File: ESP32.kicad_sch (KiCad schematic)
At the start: 5 parts, among them U6 ESP32-WROOM-32

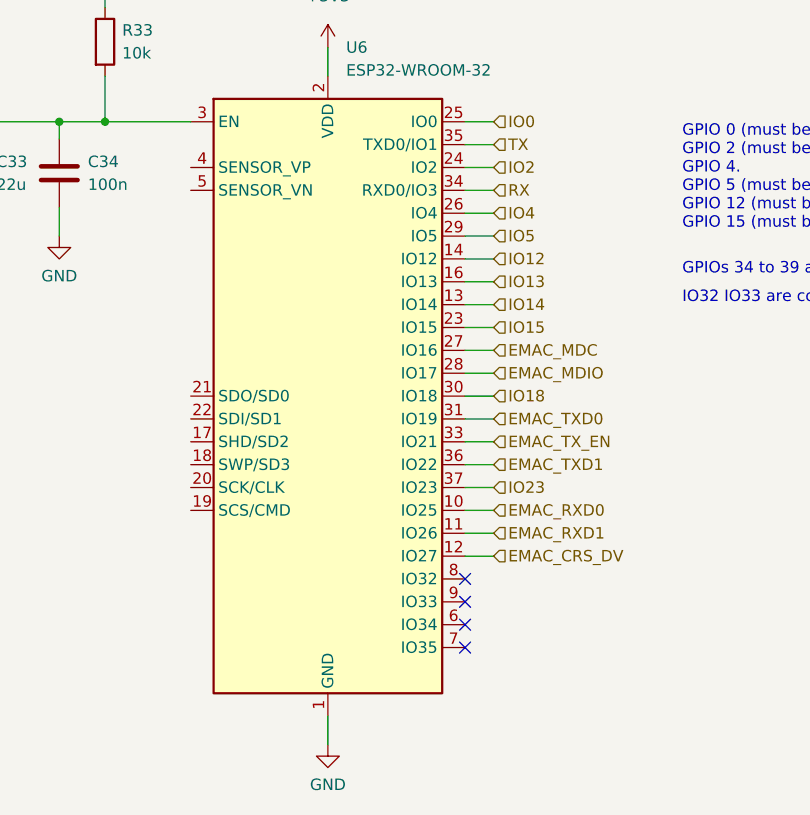
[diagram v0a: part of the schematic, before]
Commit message: Update schematic for V1.1
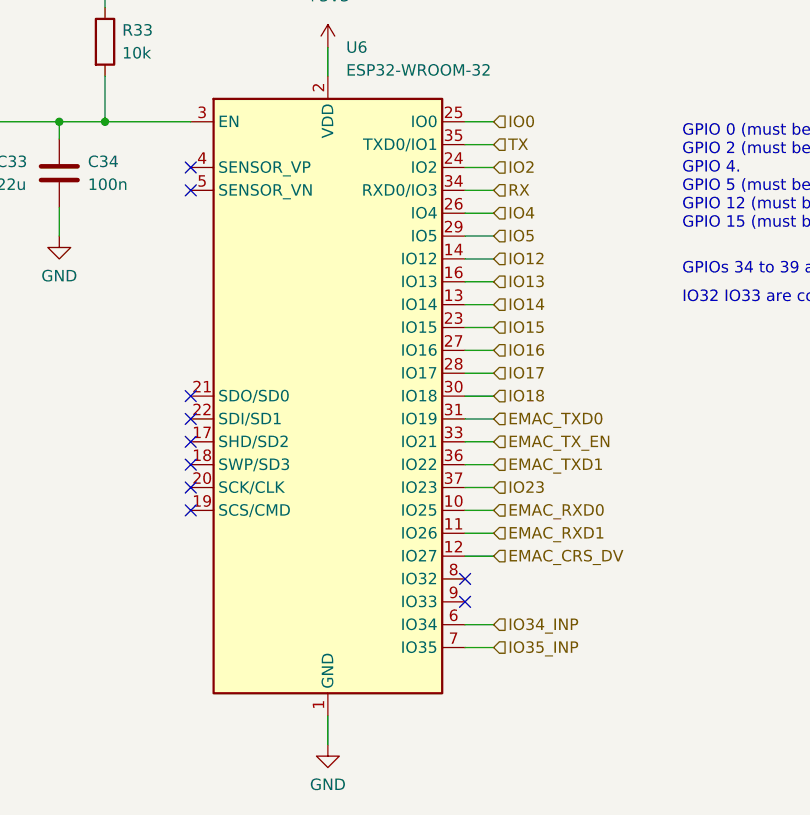
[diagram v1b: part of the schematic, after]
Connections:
- net IO34_INP: now reaches U6.6 (IO34)
- net IO35_INP: now reaches U6.7 (IO35)
- net EMAC_MDC renamed IO16
- net EMAC_MDIO renamed IO17
- no-connect marks 4 -> 10
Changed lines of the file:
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@@
 	)
 	(no_connect
-		(at 160.02 119.38)
-	)
-	(no_connect
-		(at 160.02 121.92)
+		(at 129.54 96.52)
+	)
+	(no_connect
+		(at 129.54 104.14)
 	)
 	(no_connect
@@
 	)
 	(no_connect
+		(at 129.54 101.6)
+	)
+	(no_connect
+		(at 129.54 71.12)
+	)
+	(no_connect
+		(at 129.54 93.98)
+	)
+	(no_connect
+		(at 129.54 106.68)
+	)
+	(no_connect
 		(at 160.02 114.3)
 	)
+	(no_connect
+		(at 129.54 99.06)
+	)
+	(no_connect
+		(at 129.54 68.58)
+	)
 	(wire
 		(pts
@@
 	(wire
 		(pts
+			(xy 163.195 121.92) (xy 160.02 121.92)
+		)
+		(stroke
+			(width 0)
+			(type default)
+		)
+	)
+	(wire
+		(pts
 			(xy 160.02 83.82) (xy 163.195 83.82)
+		)
+		(stroke
+			(width 0)
+			(type default)
+		)
+	)
+	(wire
+		(pts
+			(xy 160.02 119.38) (xy 163.195 119.38)
 		)
 		(stroke
@@
 		)
 	)
+	(hierarchical_label "IO34_INP"
+		(shape input)
+		(at 163.195 119.38 0)
+		(fields_autoplaced yes)
+		(effects
+			(font
+				(size 1.27 1.27)
+			)
+			(justify left)
+		)
+	)
 	(hierarchical_label "IO13"
 		(shape input)
@@
 		)
 	)
-	(hierarchical_label "EMAC_MDC"
+	(hierarchical_label "IO16"
 		(shape input)
 		(at 163.195 88.9 0)
@@
 		)
 	)
+	(hierarchical_label "IO35_INP"
+		(shape input)
+		(at 163.195 121.92 0)
+		(fields_autoplaced yes)
+		(effects
+			(font
+				(size 1.27 1.27)
+			)
+			(justify left)
+		)
+	)
 	(hierarchical_label "IO15"
 		(shape input)
@@
 		)
 	)
-	(hierarchical_label "EMAC_MDIO"
+	(hierarchical_label "IO17"
 		(shape input)
 		(at 163.195 91.44 0)

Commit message: Zamkonator rev 1.3
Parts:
- renumbered C32 to C34, C33 to C35, C34 to C36, R33 to R31, U6 to U7
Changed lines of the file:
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@@
 		(dnp no)
 		(fields_autoplaced yes)
-		(property "Reference" "#PWR047"
+		(property "Reference" "#PWR086"
 			(at 144.78 59.055 0)
 			(hide yes)
@@
 			(project "Zamkonator"
 				(path "/727d6c0a-a0ef-4feb-9656-3db3cb90564a/1f5389b7-4e7a-4b56-a78a-6bd1340c573b"
-					(reference "#PWR047")
+					(reference "#PWR086")
 					(unit 1)
 				)
@@
 		(dnp no)
 		(fields_autoplaced yes)
-		(property "Reference" "C34"
+		(property "Reference" "C36"
 			(at 118.11 67.9449 0)
 			(show_name no)
@@
 			(project "Zamkonator"
 				(path "/727d6c0a-a0ef-4feb-9656-3db3cb90564a/1f5389b7-4e7a-4b56-a78a-6bd1340c573b"
-					(reference "C34")
+					(reference "C36")
 					(unit 1)
 				)
@@
 		(dnp no)
 		(fields_autoplaced yes)
-		(property "Reference" "#PWR0109"
+		(property "Reference" "#PWR085"
 			(at 120.015 51.435 0)
 			(hide yes)
@@
 			(project "Zamkonator"
 				(path "/727d6c0a-a0ef-4feb-9656-3db3cb90564a/1f5389b7-4e7a-4b56-a78a-6bd1340c573b"
-					(reference "#PWR0109")
+					(reference "#PWR085")
 					(unit 1)
 				)
@@
 		(dnp no)
 		(fields_autoplaced yes)
-		(property "Reference" "R33"
+		(property "Reference" "R31"
 			(at 121.92 53.3399 0)
 			(show_name no)
@@
 			(project "Zamkonator"
 				(path "/727d6c0a-a0ef-4feb-9656-3db3cb90564a/1f5389b7-4e7a-4b56-a78a-6bd1340c573b"
-					(reference "R33")
+					(reference "R31")
 					(unit 1)
 				)
@@
 		(dnp no)
 		(fields_autoplaced yes)
-		(property "Reference" "#PWR044"
+		(property "Reference" "#PWR082"
 			(at 88.265 116.205 0)
 			(hide yes)
@@
 			(project "Zamkonator"
 				(path "/727d6c0a-a0ef-4feb-9656-3db3cb90564a/1f5389b7-4e7a-4b56-a78a-6bd1340c573b"
-					(reference "#PWR044")
+					(reference "#PWR082")
 					(unit 1)
 				)
@@
 		(dnp no)
 		(fields_autoplaced yes)
-		(property "Reference" "#PWR046"
+		(property "Reference" "#PWR084"
 			(at 114.935 82.55 0)
 			(hide yes)
@@
 			(project "Zamkonator"
 				(path "/727d6c0a-a0ef-4feb-9656-3db3cb90564a/1f5389b7-4e7a-4b56-a78a-6bd1340c573b"
-					(reference "#PWR046")
+					(reference "#PWR084")
 					(unit 1)
 				)
@@
 		(dnp no)
 		(fields_autoplaced yes)
-		(property "Reference" "C33"
+		(property "Reference" "C35"
 			(at 107.95 67.9449 0)
 			(show_name no)
@@
 			(project "Zamkonator"
 				(path "/727d6c0a-a0ef-4feb-9656-3db3cb90564a/1f5389b7-4e7a-4b56-a78a-6bd1340c573b"
-					(reference "C33")
+					(reference "C35")
 					(unit 1)
 				)
@@
 		(dnp no)
 		(fields_autoplaced yes)
-		(property "Reference" "U6"
+		(property "Reference" "U7"
 			(at 146.7994 55.245 0)
 			(show_name no)
@@
 			(project "Zamkonator"
 				(path "/727d6c0a-a0ef-4feb-9656-3db3cb90564a/1f5389b7-4e7a-4b56-a78a-6bd1340c573b"
-					(reference "U6")
+					(reference "U7")
 					(unit 1)
 				)
@@
 		(dnp no)
 		(fields_autoplaced yes)
-		(property "Reference" "C32"
+		(property "Reference" "C34"
 			(at 92.075 101.5999 0)
 			(show_name no)
@@
 			(project "Zamkonator"
 				(path "/727d6c0a-a0ef-4feb-9656-3db3cb90564a/1f5389b7-4e7a-4b56-a78a-6bd1340c573b"
-					(reference "C32")
+					(reference "C34")
 					(unit 1)
 				)
@@
 		(dnp no)
 		(fields_autoplaced yes)
-		(property "Reference" "#PWR045"
+		(property "Reference" "#PWR083"
 			(at 104.775 82.55 0)
 			(hide yes)
@@
 			(project "Zamkonator"
 				(path "/727d6c0a-a0ef-4feb-9656-3db3cb90564a/1f5389b7-4e7a-4b56-a78a-6bd1340c573b"
-					(reference "#PWR045")
+					(reference "#PWR083")
 					(unit 1)
 				)
@@
 		(dnp no)
 		(fields_autoplaced yes)
-		(property "Reference" "#PWR043"
+		(property "Reference" "#PWR081"
 			(at 88.265 98.425 0)
 			(hide yes)
@@
 			(project "Zamkonator"
 				(path "/727d6c0a-a0ef-4feb-9656-3db3cb90564a/1f5389b7-4e7a-4b56-a78a-6bd1340c573b"
-					(reference "#PWR043")
+					(reference "#PWR081")
 					(unit 1)
 				)
@@
 		(dnp no)
 		(fields_autoplaced yes)
-		(property "Reference" "#PWR048"
+		(property "Reference" "#PWR087"
 			(at 144.78 139.065 0)
 			(hide yes)
@@
 			(project "Zamkonator"
 				(path "/727d6c0a-a0ef-4feb-9656-3db3cb90564a/1f5389b7-4e7a-4b56-a78a-6bd1340c573b"
-					(reference "#PWR048")
+					(reference "#PWR087")
 					(unit 1)
 				)

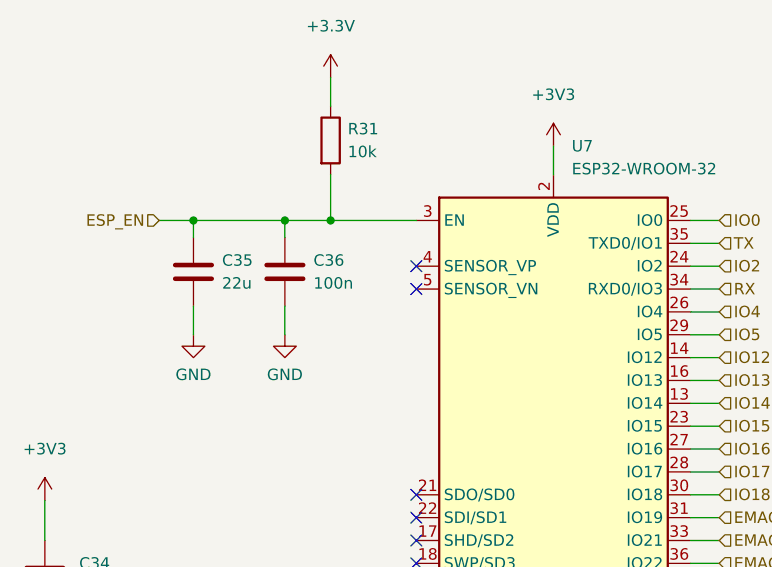
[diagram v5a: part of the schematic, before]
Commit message: Rev 1.3, BOM optimizations
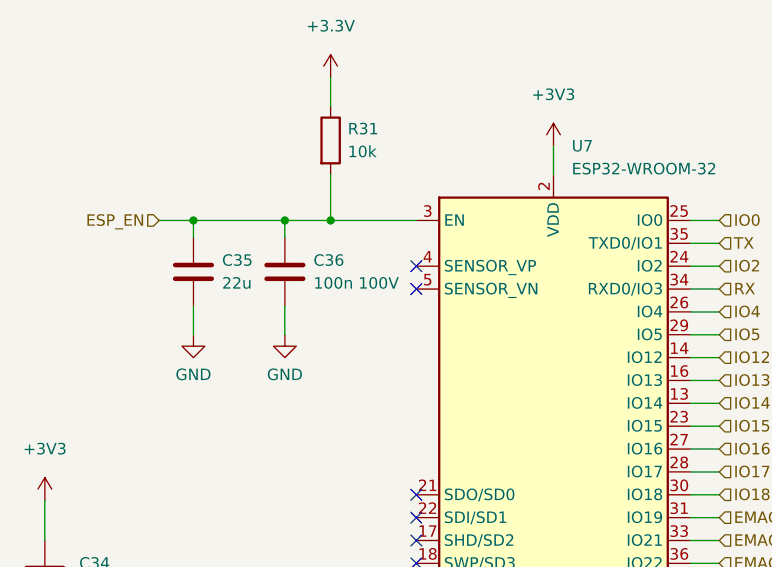
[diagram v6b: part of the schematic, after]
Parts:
- C36: value 100n -> 100n 100V
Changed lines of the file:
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@@
 			)
 		)
-		(property "Value" "100n"
+		(property "Value" "100n 100V"
 			(at 118.11 70.4849 0)
 			(show_name no)
